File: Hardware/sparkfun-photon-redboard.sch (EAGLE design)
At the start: 54 parts, among them U1 WM-N-BM-14

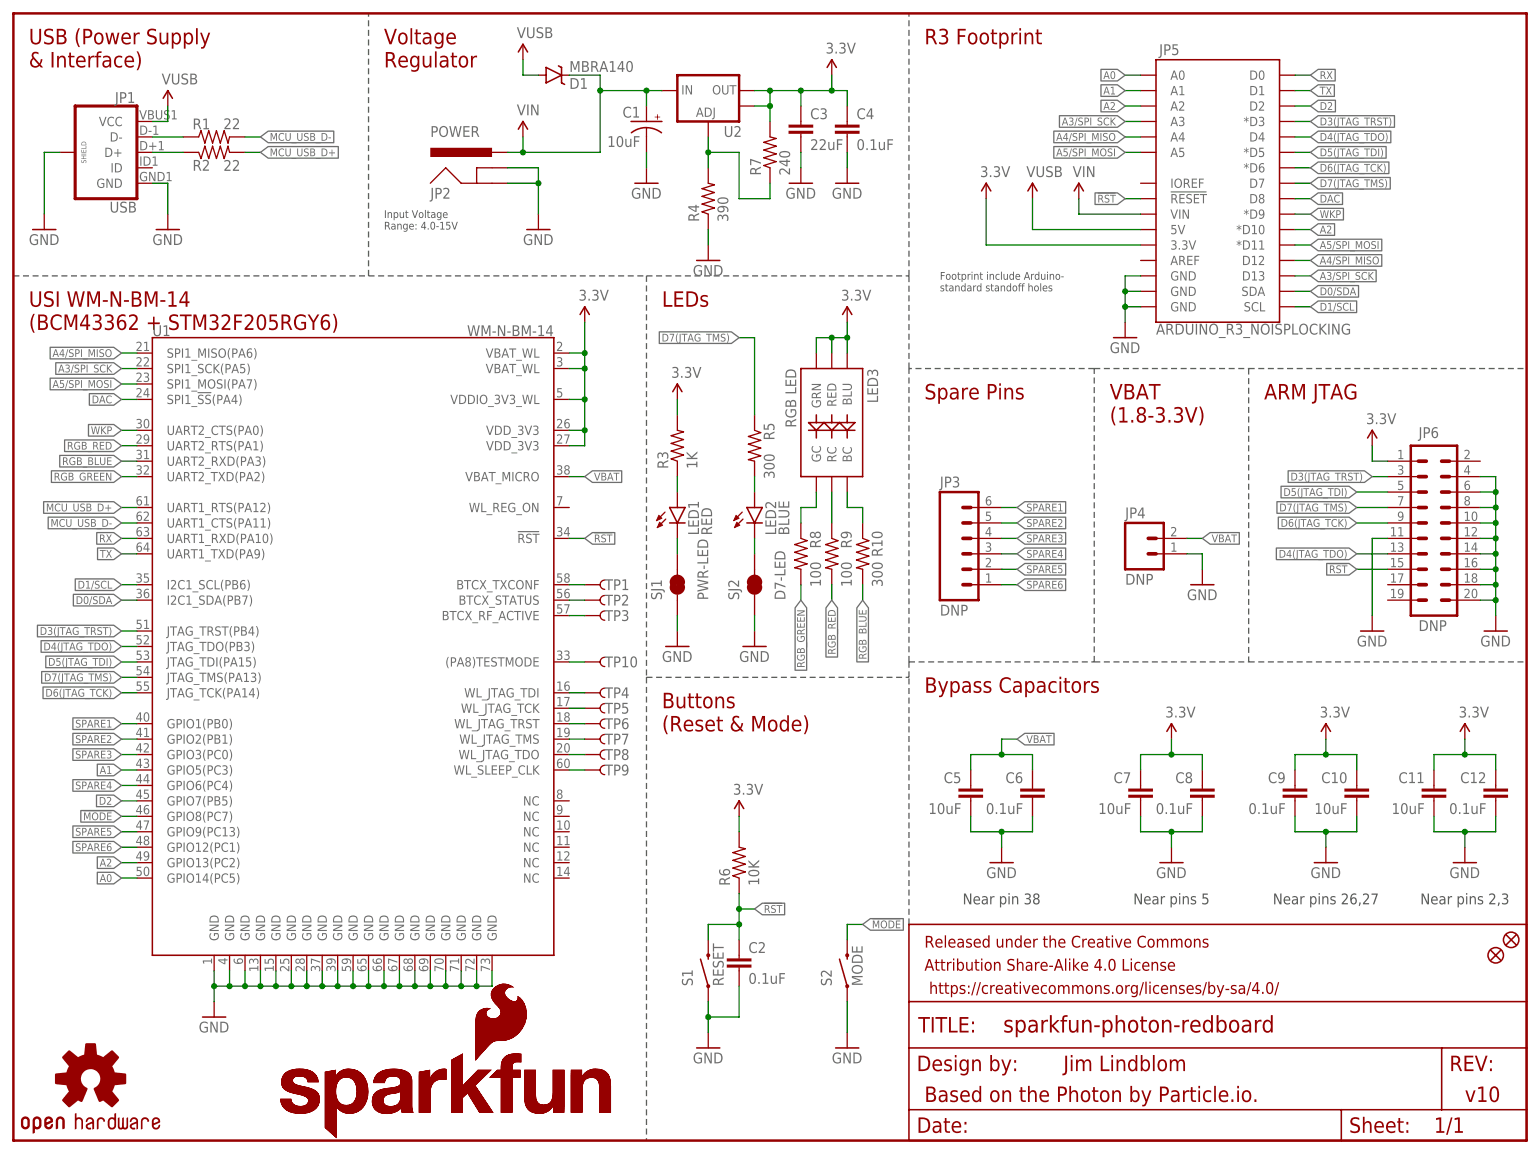
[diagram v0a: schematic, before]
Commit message: Switched RGB LED and resistor values
-Previous RGB was EOL
-changed resistor values to match existing proven designs (100/100/220)
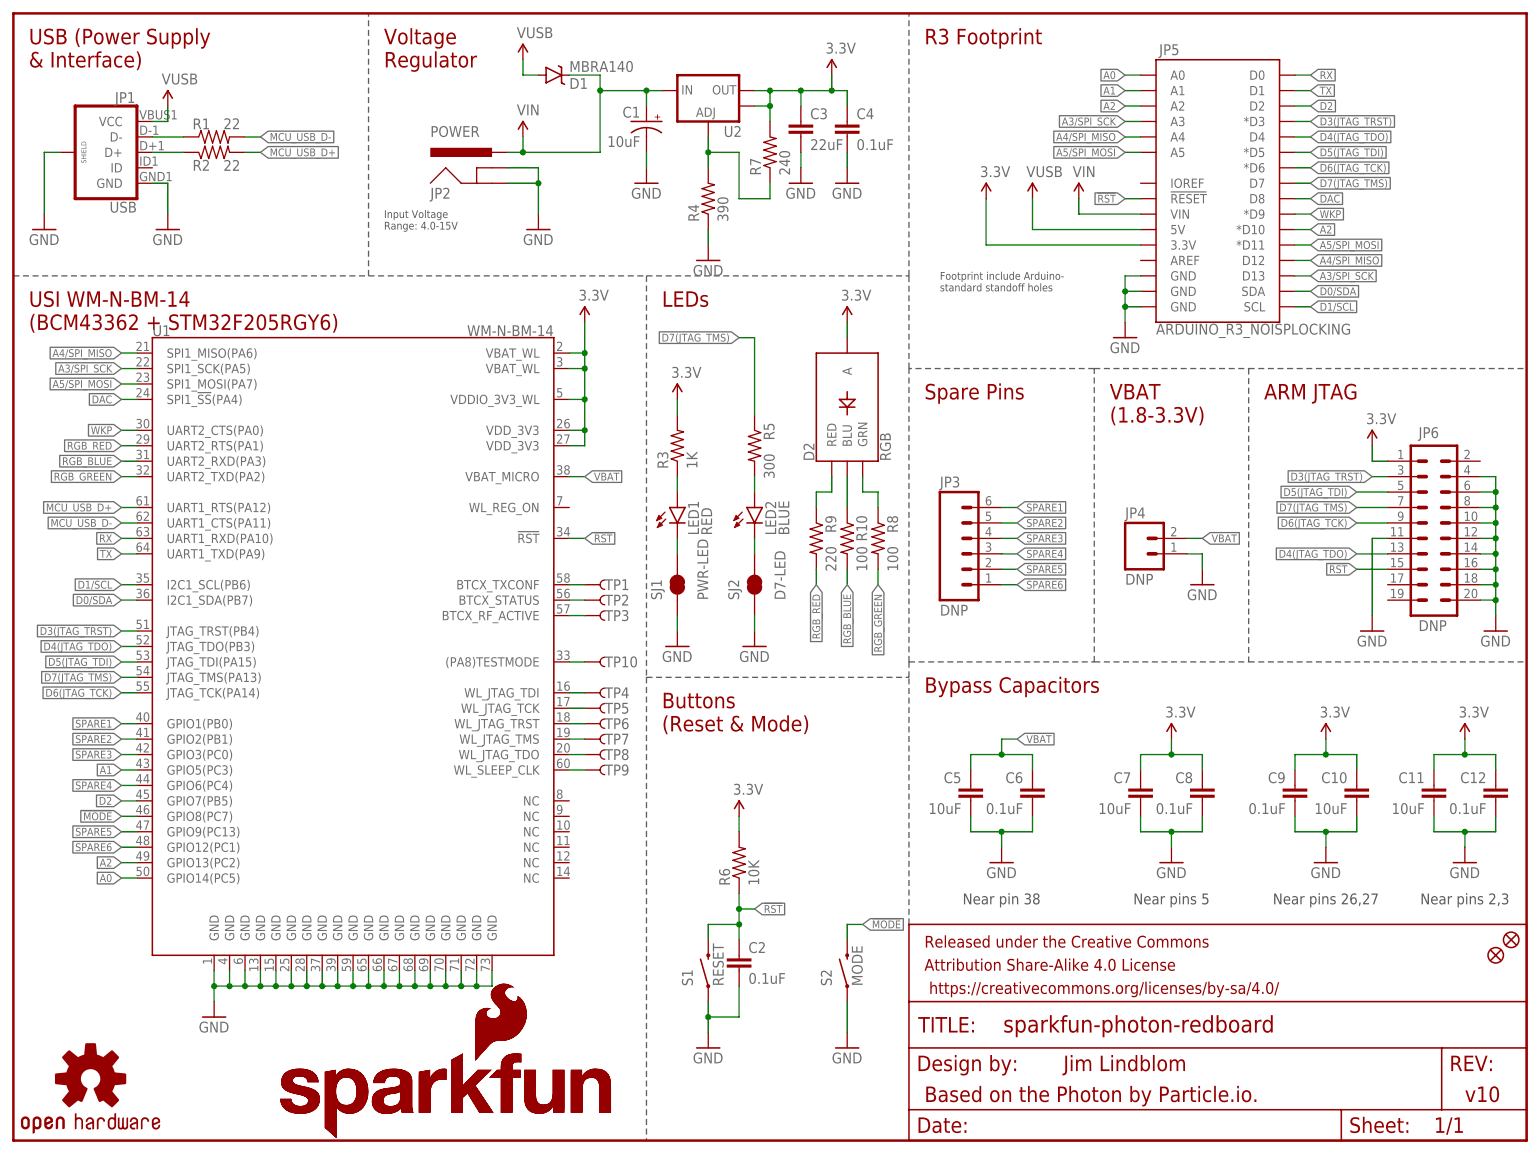
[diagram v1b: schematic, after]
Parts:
- removed LED3: RGB LED, SparkFun-LED:LED-TRICOLOR-NO-COMPLCC-6-SMD
- added D2: RGB, SparkFun-LED:LED-RGB-CAPLCC
- R10: value 300 -> 100; device SparkFun-Resistors:300OHM-1/10W-1%(0603) -> SparkFun-Resistors:100OHM-0603-1/10W-1%
- R9: value 100 -> 220; device SparkFun-Resistors:100OHM-1/10W-1%(0603) -> SparkFun-Resistors:220OHM-0603-1/10W-1%
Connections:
- removed net N$5: LED3.BC, R10.1
- new net N$9: D2.BLU, R10.1
- net 3.3V: now also D2.A; no longer LED3.BLU, LED3.GRN, LED3.RED
- net N$3: now also D2.GRN; no longer LED3.GC
- net N$4: now also D2.RED; no longer LED3.RC
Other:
- moved on the sheet: R10, R8, R9

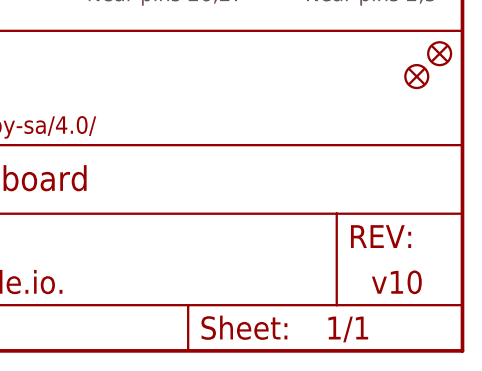
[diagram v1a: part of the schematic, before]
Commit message: updated version to "v11" in bottom copper and sch
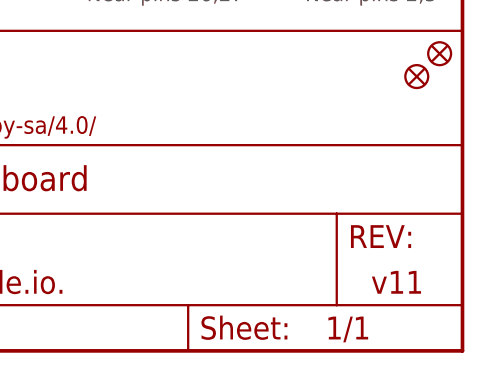
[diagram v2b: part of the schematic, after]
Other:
- note added: "v11"
- note removed: "v10"
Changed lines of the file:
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@@
 <text x="149.86" y="7.62" size="2.54" layer="94" align="center-left">Based on the Photon by Particle.io.</text>
 <text x="172.72" y="12.7" size="2.54" layer="94" align="center-left">Jim Lindblom</text>
-<text x="238.76" y="7.62" size="2.54" layer="94" align="center-left">v10</text>
+<text x="238.76" y="7.62" size="2.54" layer="94" align="center-left">v11</text>
 <text x="60.96" y="149.86" size="1.27" layer="97">Input Voltage
 Range: 4.0-15V</text>
